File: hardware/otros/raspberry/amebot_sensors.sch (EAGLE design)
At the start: 17 parts

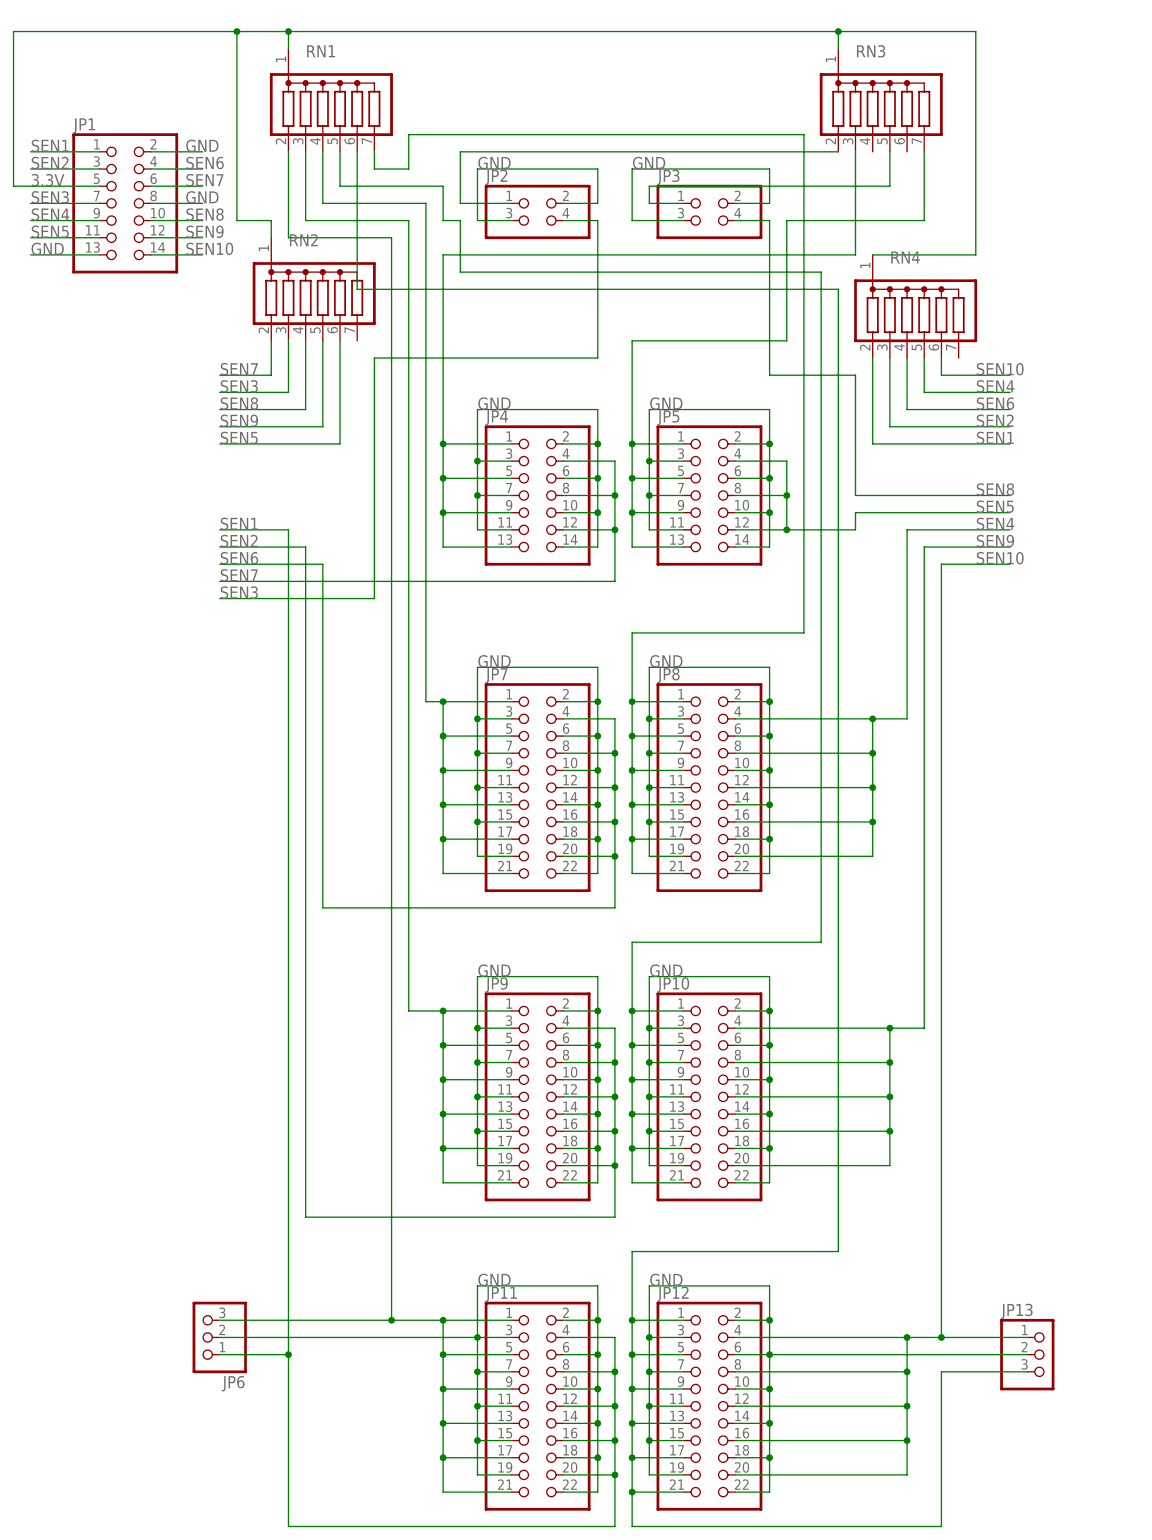
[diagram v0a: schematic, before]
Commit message: cambio el común por 3.3V en lugar de masa
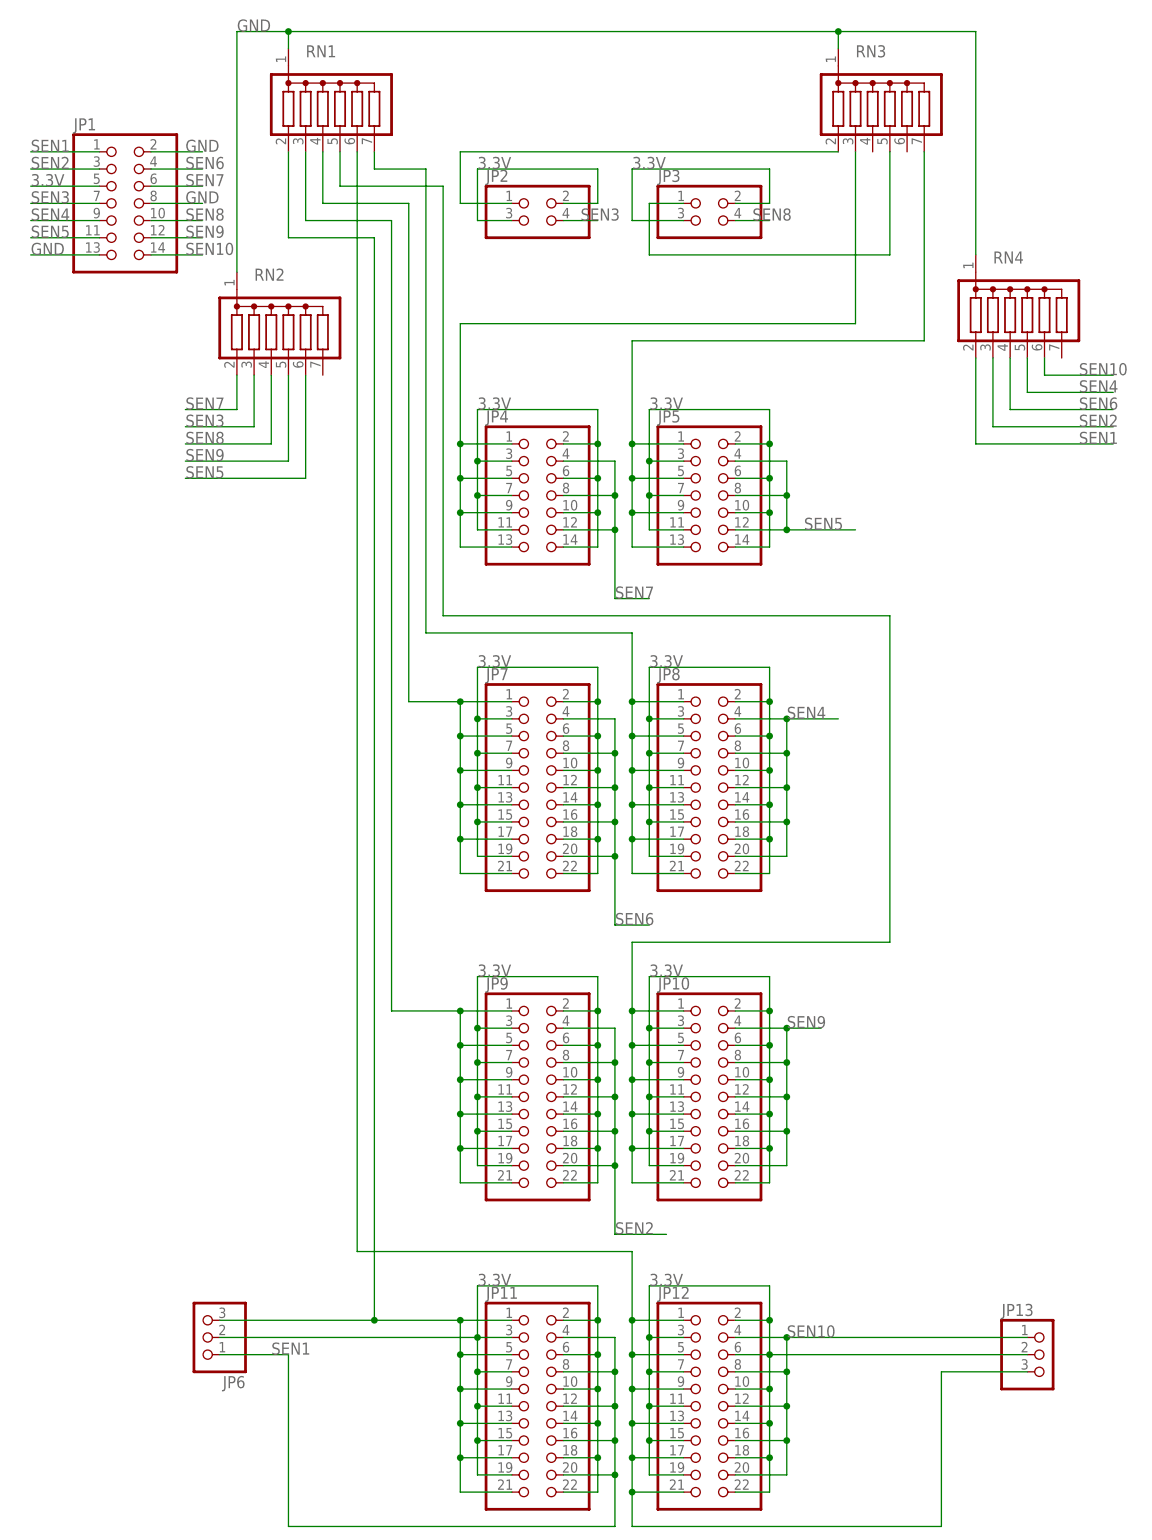
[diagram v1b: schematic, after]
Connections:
- net 3.3V: now also JP10.10, JP10.11, JP10.14, JP10.15, JP10.18, JP10.19, JP10.2, JP10.22, JP10.3, JP10.6, JP10.7, JP11.10, JP11.11, JP11.14, JP11.15, JP11.18, JP11.19, JP11.2, JP11.22, JP11.3, JP11.6, JP11.7, JP12.10, JP12.11, JP12.14, JP12.15, JP12.18, JP12.19, JP12.2, JP12.22, JP12.3, JP12.6, JP12.7, JP13.2, JP2.2, JP2.3, JP3.2, JP3.3, JP4.10, JP4.11, JP4.14, JP4.2, JP4.3, JP4.6, JP4.7, JP5.10, JP5.11, JP5.14, JP5.2, JP5.3, JP5.6, JP5.7, JP6.2, JP7.10, JP7.11, JP7.14, JP7.15, JP7.18, JP7.19, JP7.2, JP7.22, JP7.3, JP7.6, JP7.7, JP8.10, JP8.11, JP8.14, JP8.15, JP8.18, JP8.19, JP8.2, JP8.22, JP8.3, JP8.6, JP8.7, JP9.10, JP9.11, JP9.14, JP9.15, JP9.18, JP9.19, JP9.2, JP9.22, JP9.3, JP9.6, JP9.7; no longer RN1.1, RN2.1, RN3.1, RN4.1
- net GND: now also RN1.1, RN2.1, RN3.1, RN4.1; no longer JP10.10, JP10.11, JP10.14, JP10.15, JP10.18, JP10.19, JP10.2, JP10.22, JP10.3, JP10.6, JP10.7, JP11.10, JP11.11, JP11.14, JP11.15, JP11.18, JP11.19, JP11.2, JP11.22, JP11.3, JP11.6, JP11.7, JP12.10, JP12.11, JP12.14, JP12.15, JP12.18, JP12.19, JP12.2, JP12.22, JP12.3, JP12.6, JP12.7, JP13.2, JP2.2, JP2.3, JP3.2, JP3.3, JP4.10, JP4.11, JP4.14, JP4.2, JP4.3, JP4.6, JP4.7, JP5.10, JP5.11, JP5.14, JP5.2, JP5.3, JP5.6, JP5.7, JP6.2, JP7.10, JP7.11, JP7.14, JP7.15, JP7.18, JP7.19, JP7.2, JP7.22, JP7.3, JP7.6, JP7.7, JP8.10, JP8.11, JP8.14, JP8.15, JP8.18, JP8.19, JP8.2, JP8.22, JP8.3, JP8.6, JP8.7, JP9.10, JP9.11, JP9.14, JP9.15, JP9.18, JP9.19, JP9.2, JP9.22, JP9.3, JP9.6, JP9.7
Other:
- moved on the sheet: RN2, RN4
